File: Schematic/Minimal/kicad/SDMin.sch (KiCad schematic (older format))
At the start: 89 parts

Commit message: Update schematic, order capacitors/resistors/headers and list their size in HW
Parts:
- removed C?: 4.7uF, symbol C_Small
- removed C?: 0.22uF, symbol C_Small
- removed C?: 10uF, symbol C_Small
- removed C?: 100nF, symbol C_Small
- removed SW? (x7): SW_PUSH, symbol SW_PUSH
- removed U?: LSM303DTR, symbol LSM303DTR
- added SW2, SW3, SW4, SW6, SW7, SW8, SW9: SW_PUSH, Buttons_Switches_ThroughHole:SW_PUSH_SMALL, symbol SW_PUSH
- C1, C2: renamed from C?; footprint (none) -> Capacitors_ThroughHole:C_Radial_D5_L11_P2.5
- C11, C13, C15, C4, C7: renamed from C?; value 100nF -> 0.1uF
- C27: renamed from C?; value 4700pF -> 4.7nF
- SW1: renamed from SW?; footprint (none) -> Buttons_Switches_ThroughHole:SW_PUSH_SMALL
- U12: renamed from U?; footprint (none) -> Housings_SOIC:SOIC-28_7.5x17.9mm_Pitch1.27mm
- U8: renamed from U?; footprint (none) -> Housings_DFN_QFN:QFN-16-1EP_3x3mm_Pitch0.5mm
- gave numbers to parts that had none: 66
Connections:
- net labels removed: PB12_MAG-INT1, PB13_MAG-INT2, PB15_MAG-SDI, PB3_dbg, PC2_MAG-SDO
- wire segments 294 -> 262
- no-connect marks 0 -> 39

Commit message: Finish schematic, finish drawing footprints, associate all parts to footprints, get a reading from the GPS.
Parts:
- added C30: 0.1uF, Capacitors_SMD:C_0805_HandSoldering, symbol C_Small
- BT1: footprint (none) -> con-trougnouf:18650BatteryHolder
- C10, C12, C14, C16, C17, C3, C5, C6, C8, C9: footprint (none) -> Capacitors_ThroughHole:C_Radial_D5_L11_P2.5
- C11, C13, C15, C19, C20, C21, C22, C23, C24, C25, C26, C27, C28, C29, C4, C7: footprint (none) -> Capacitors_SMD:C_0805_HandSoldering
- C18: value 100nF -> 0.1uF; footprint (none) -> Capacitors_SMD:C_0805_HandSoldering
- CON1: value SD_Card -> uSD_Card; footprint 10067847-001 -> con-trougnouf:MicroSD; symbol SD_Card -> uSD_Card
- D1, D2, D3: footprint (none) -> LEDs:LED_0603
- L1: value 4.7uF -> 4.7uH; footprint (none) -> Inductors_NEOSID:Neosid_Inductor_SM-NE29_SMD1008
- L2: footprint (none) -> Inductors_NEOSID:Neosid_Inductor_SM-NE29_SMD1008
- P2, P3, P4: footprint (none) -> Pin_Headers:Pin_Header_Straight_1x04
- R1, R10, R11, R12, R13, R14, R15, R16, R17, R18, R19, R2, R20, R21, R22, R3, R4, R5, R6, R7, R8, R9: footprint (none) -> Resistors_SMD:R_0805_HandSoldering
- U10: footprint (none) -> Pin_Headers:Pin_Header_Straight_1x03
- U11: footprint (none) -> BT:RN-52
- U7: footprint Pin_Headers:Pin_Header_Straight_1x05 -> Pin_Headers:Pin_Header_Straight_1x04
- U9: footprint (none) -> Pin_Headers:Pin_Header_Straight_1x05
- X1: footprint (none) -> Crystals:Crystal_HC49-SD_SMD
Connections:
- wire segments 262 -> 263
- no-connect marks 39 -> 38

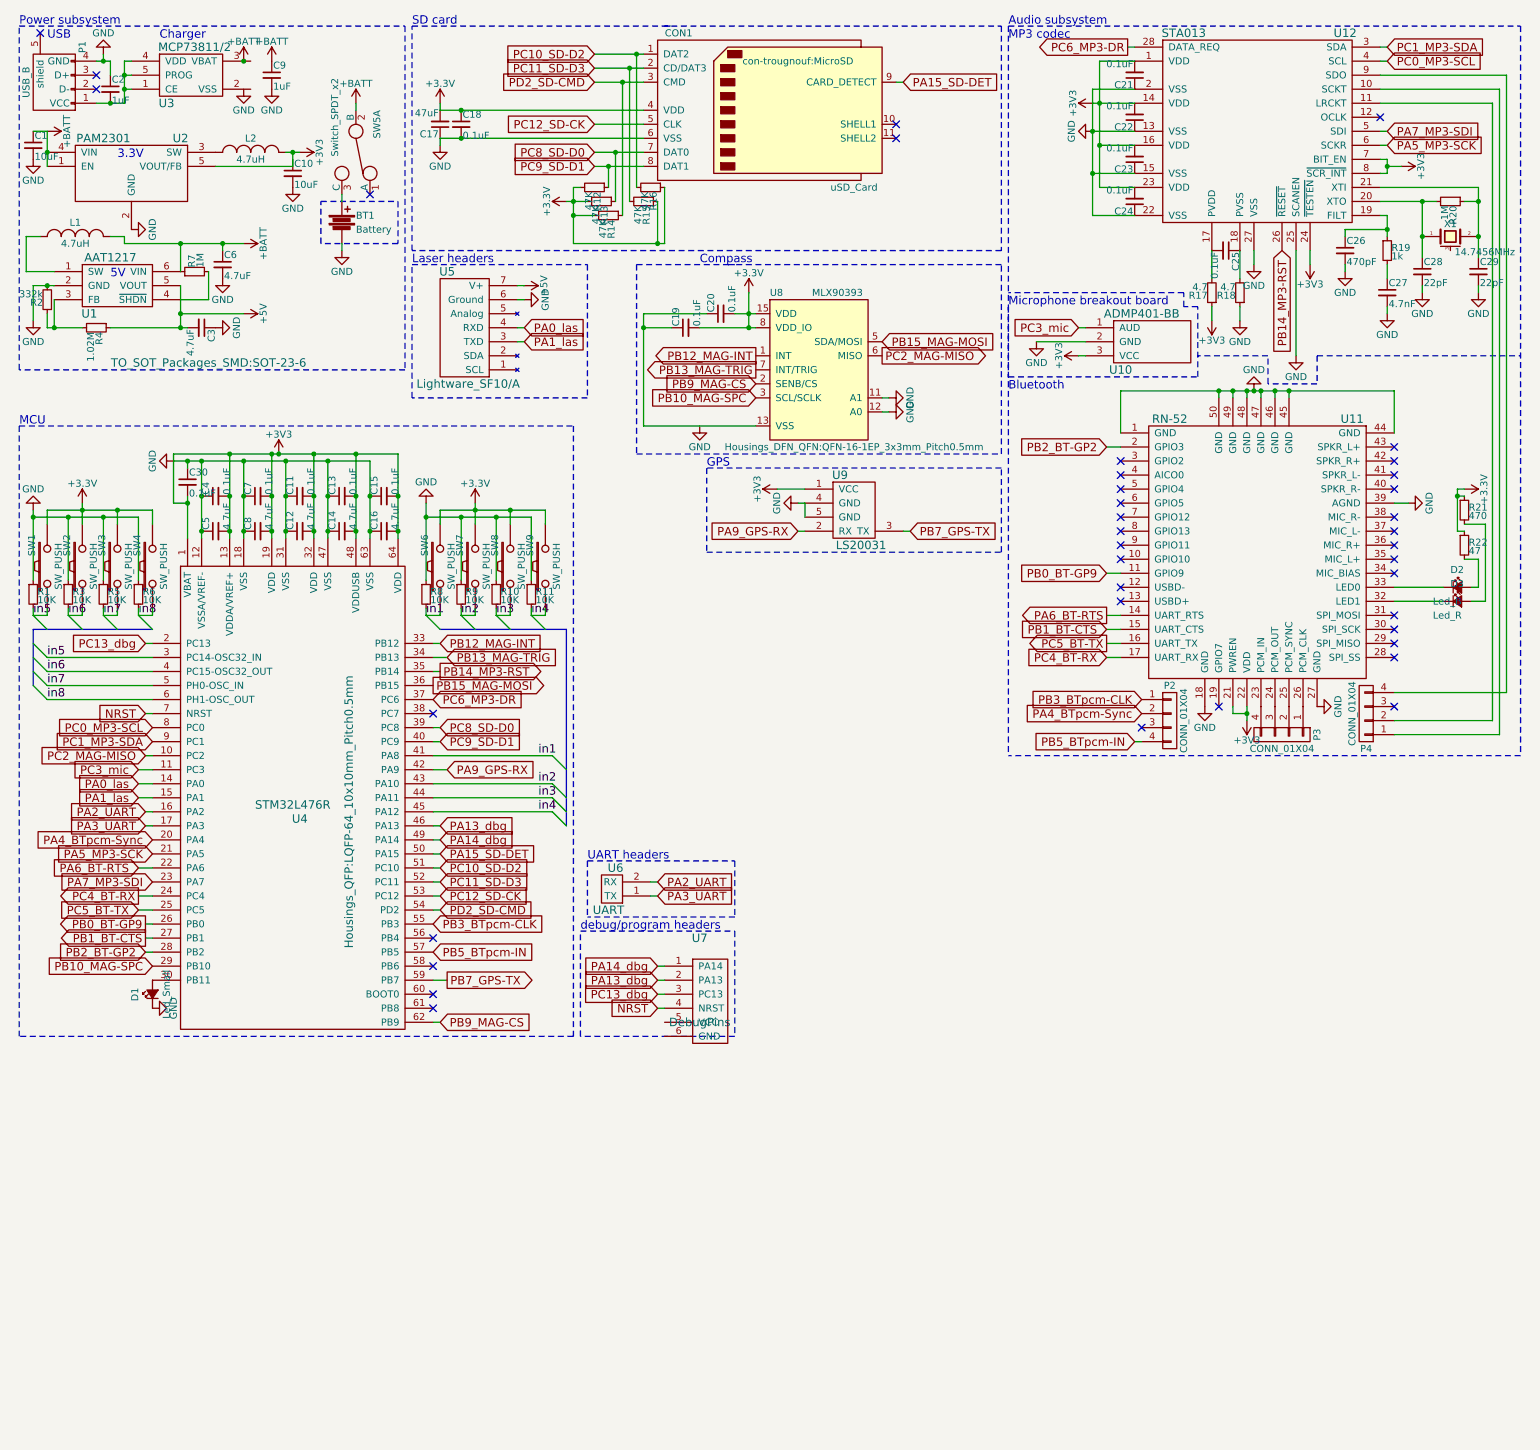
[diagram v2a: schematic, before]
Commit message: Working on the PCB (third attempt). Misc schematic fixes (charger always on)
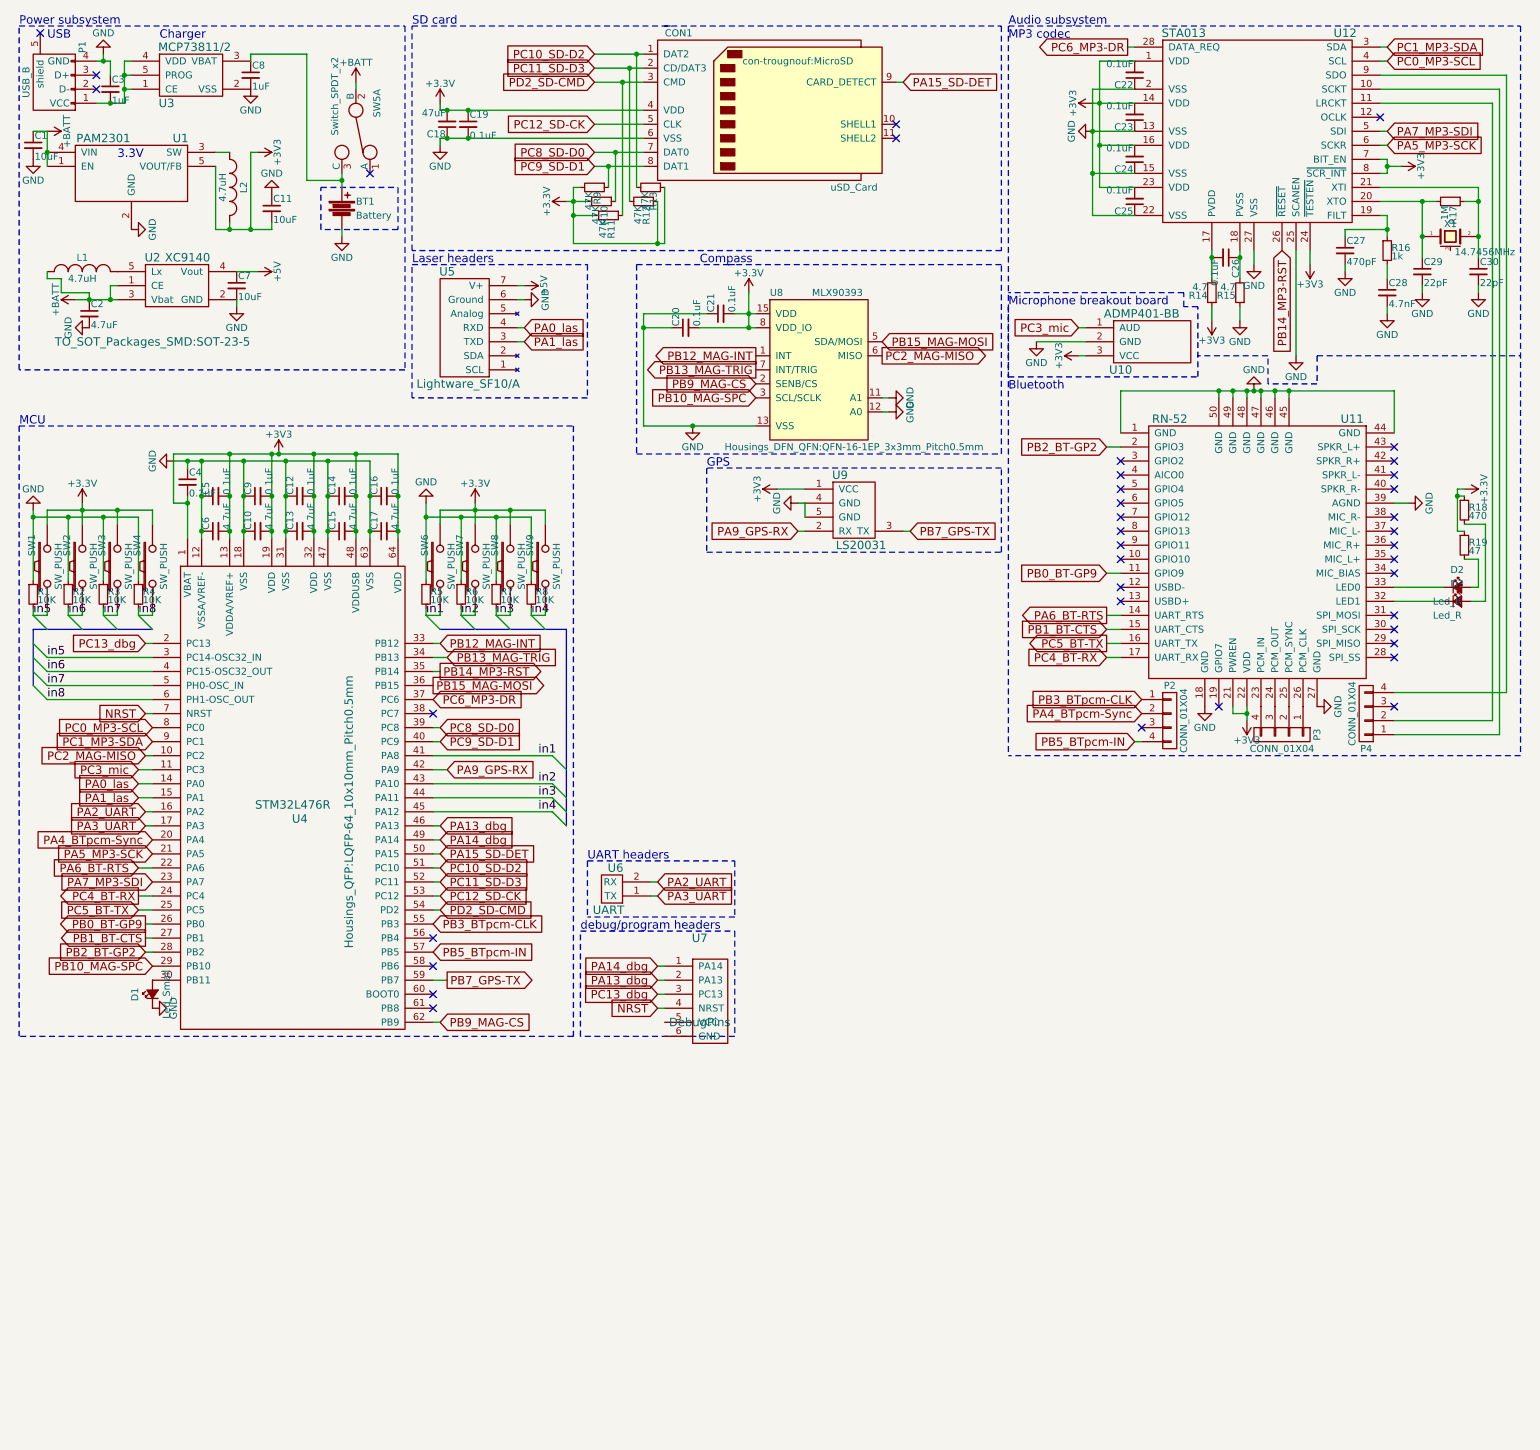
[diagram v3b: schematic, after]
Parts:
- removed C3, C6: 4.7uF, Capacitors_ThroughHole:C_Radial_D5_L11_P2.5, symbol C_Small
- removed R2: 332k, Resistors_SMD:R_0805_HandSoldering, symbol R_Small
- removed R4: 1.02M, Resistors_SMD:R_0805_HandSoldering, symbol R_Small
- removed R7: 1M, Resistors_SMD:R_0805_HandSoldering, symbol R_Small
- removed U1: AAT1217, TO_SOT_Packages_SMD:SOT-23-6, symbol AAT1217
- added C2: 4.7uF, Capacitors_SMD:C_0805_HandSoldering, symbol C_Small
- added C7: 10uF, Capacitors_SMD:C_0805_HandSoldering, symbol C_Small
- added U2: XC9140, TO_SOT_Packages_SMD:SOT-23-5, symbol XC9140
- U10: footprint Pin_Headers:Pin_Header_Straight_1x03 -> con-trougnouf:INMP401-bb
- U9: footprint Pin_Headers:Pin_Header_Straight_1x05 -> con-trougnouf:LS20031+H
- renumbered C8 to C10, C10 to C11, C11 to C12, C12 to C13, C13 to C14, C14 to C15, C15 to C16, C16 to C17, C17 to C18, C18 to C19, C19 to C20, C20 to C21, C21 to C22, C22 to C23, C23 to C24, C24 to C25, C25 to C26, C26 to C27, C27 to C28, C28 to C29, C2 to C3, C29 to C30, C30 to C4, C4 to C5, C5 to C6, C9 to C8, C7 to C9, R13 to R10, R14 to R11, R15 to R12, R16 to R13, R17 to R14, R18 to R15, R19 to R16, R20 to R17, R21 to R18, R22 to R19, R3 to R2, R5 to R3, R6 to R4, R8 to R5, R9 to R6, R10 to R7, R11 to R8, R12 to R9, U2 to U1
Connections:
- net +3V3: now also C11.2
- net +5V: now also C7.1, U2.4 (Vout)
- net +BATT: now also L1.1, C2.1, U2.1 (CE), U2.3 (Vbat); no longer C8.1, L1.2
- net GND: now also C11.1, C20.1, C21.1, U3.2 (VSS), U8.13 (VSS), C2.2, C7.2, U2.2 (GND); no longer C11.2
- net at BT1.1, SW5.3 (C): now also C8.1, U3.3 (VBAT)
- new net: L1.2, U2.5 (Lx)
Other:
- note removed: "5V"
- moved on the sheet: BT1, C11, C18, C19, C26, C8, L1, L2, SW5A

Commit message: Lots of progress on the mPCB
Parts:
- removed SW5: Switch_SPDT_x2, Buttons_Switches_ThroughHole:SW_Micro_SPST, symbol Switch_SPDT_x2
- added C31: 0.1uF, Capacitors_SMD:C_0805_HandSoldering, symbol C_Small
- added P5: CONN_01X03, Pin_Headers:Pin_Header_Straight_1x03, symbol CONN_01X03
- added P6: CONN_01X02, Socket_Strips:Socket_Strip_Straight_1x02, symbol CONN_01X02
- added R20: 10K, Resistors_SMD:R_0805_HandSoldering, symbol R_Small
- added SW5: SW_PUSH, Buttons_Switches_ThroughHole:SW_PUSH_SMALL, symbol SW_PUSH
- U6: footprint Pin_Headers:Pin_Header_Straight_1x02 -> Socket_Strips:Socket_Strip_Straight_1x02
- U7: footprint Pin_Headers:Pin_Header_Straight_1x04 -> Socket_Strips:Socket_Strip_Straight_1x06
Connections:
- net +3V3: now also U7.5 (VCC), C31.2, R20.1
- net +BATT: now also BT1.1, C8.1, U3.3 (VBAT), P5.2 (P2); no longer C1.1, U1.1 (EN), U1.4 (VIN), U2.1 (CE)
- net GND: now also U7.6 (GND), C31.1, SW5.2
- net NRST: now also R20.2, SW5.1
- net at D1.2 (A): now also U4.61 (PB8); no longer U4.30 (PB11)
- net 5VEN: now reaches U4.38 (PC7)
- net 5VEN: now also U2.1 (CE)
- net x-in-1: now reaches U4.56 (PB4)
- net x-in-1: now also P6.2 (P2)
- net x-in-2: now reaches U4.58 (PB6)
- net x-in-2: now also P6.1 (P1)
- net PB0_BT-GP9 renamed PB0_mic
- net PB0_mic: now also U10.1 (AUD); no longer U11.11 (GPIO9)
- net PC3_mic: no longer names the net of U4.11 (PC3)
- net PC3_mic: no longer U10.1 (AUD)
- new net 3VEN: C1.1, P5.1 (P1), U1.1 (EN), U1.4 (VIN)
- new net PB11_BT-GP9: U11.11 (GPIO9), U4.30 (PB11)
- no-connect marks 38 -> 33
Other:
- moved on the sheet: BT1, C8, D1, U7

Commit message: PCB4-23
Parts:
- added C32, C33, C34: 0.1uF, Capacitors_SMD:C_0805_HandSoldering, symbol C_Small
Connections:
- net +3V3: now also C32.1, C33.1, C34.1
- net GND: now also C32.2, C33.2, C34.2
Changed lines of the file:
@@
 Wire Wire Line
 	1200 2400 1050 2400
-Text Label 4350 5450 2    60   ~ 0
+Text Label 3700 5450 2    60   ~ 0
 5VEN
-Wire Wire Line
-	3450 5450 4350 5450
 $Comp
 L R_Small R20
@@
 Connection ~ 5500 5350
 $Comp
-L +BATT #PWR?
+L +BATT #PWR055
 U 1 1 56D36626
 P 800 2450
-F 0 "#PWR?" H 800 2300 50  0001 C CNN
+F 0 "#PWR055" H 800 2300 50  0001 C CNN
 F 1 "+BATT" H 800 2590 50  0000 C CNN
 F 2 "" H 800 2450 50  0000 C CNN
@@
 	0    -1   -1   0
 $EndComp
+$Comp
+L C_Small C32
+U 1 1 56D39376
+P 5050 4550
+F 0 "C32" H 5060 4620 50  0000 L CNN
+F 1 "0.1uF" H 5060 4470 50  0000 L CNN
+F 2 "Capacitors_SMD:C_0805_HandSoldering" H 5050 4550 50  0001 C CNN
+F 3 "" H 5050 4550 50  0000 C CNN
+	1    5050 4550
+	0    -1   -1   0
+$EndComp
+$Comp
+L C_Small C33
+U 1 1 56D39874
+P 5050 4700
+F 0 "C33" H 5060 4770 50  0000 L CNN
+F 1 "0.1uF" H 5060 4620 50  0000 L CNN
+F 2 "Capacitors_SMD:C_0805_HandSoldering" H 5050 4700 50  0001 C CNN
+F 3 "" H 5050 4700 50  0000 C CNN
+	1    5050 4700
+	0    -1   -1   0
+$EndComp
+$Comp
+L +3.3V #PWR056
+U 1 1 56D39A98
+P 4900 4550
+F 0 "#PWR056" H 4900 4400 50  0001 C CNN
+F 1 "+3.3V" H 4900 4690 50  0000 C CNN
+F 2 "" H 4900 4550 50  0000 C CNN
+F 3 "" H 4900 4550 50  0000 C CNN
+	1    4900 4550
+	0    -1   -1   0
+$EndComp
+$Comp
+L +3.3V #PWR057
+U 1 1 56D39BB4
+P 4900 4700
+F 0 "#PWR057" H 4900 4550 50  0001 C CNN
+F 1 "+3.3V" H 4900 4840 50  0000 C CNN
+F 2 "" H 4900 4700 50  0000 C CNN
+F 3 "" H 4900 4700 50  0000 C CNN
+	1    4900 4700
+	0    -1   -1   0
+$EndComp
+$Comp
+L GND #PWR058
+U 1 1 56D39CD0
+P 5200 4550
+F 0 "#PWR058" H 5200 4300 50  0001 C CNN
+F 1 "GND" H 5200 4400 50  0000 C CNN
+F 2 "" H 5200 4550 50  0000 C CNN
+F 3 "" H 5200 4550 50  0000 C CNN
+	1    5200 4550
+	0    -1   -1   0
+$EndComp
+$Comp
+L GND #PWR059
+U 1 1 56D39DEC
+P 5200 4700
+F 0 "#PWR059" H 5200 4450 50  0001 C CNN
+F 1 "GND" H 5200 4550 50  0000 C CNN
+F 2 "" H 5200 4700 50  0000 C CNN
+F 3 "" H 5200 4700 50  0000 C CNN
+	1    5200 4700
+	0    -1   -1   0
+$EndComp
+$Comp
+L C_Small C34
+U 1 1 56D3A0EC
+P 5050 4850
+F 0 "C34" H 5060 4920 50  0000 L CNN
+F 1 "0.1uF" H 5060 4770 50  0000 L CNN
+F 2 "Capacitors_SMD:C_0805_HandSoldering" H 5050 4850 50  0001 C CNN
+F 3 "" H 5050 4850 50  0000 C CNN
+	1    5050 4850
+	0    -1   -1   0
+$EndComp
+$Comp
+L +3.3V #PWR060
+U 1 1 56D3A0F2
+P 4900 4850
+F 0 "#PWR060" H 4900 4700 50  0001 C CNN
+F 1 "+3.3V" H 4900 4990 50  0000 C CNN
+F 2 "" H 4900 4850 50  0000 C CNN
+F 3 "" H 4900 4850 50  0000 C CNN
+	1    4900 4850
+	0    -1   -1   0
+$EndComp
+$Comp
+L GND #PWR061
+U 1 1 56D3A0F8
+P 5200 4850
+F 0 "#PWR061" H 5200 4600 50  0001 C CNN
+F 1 "GND" H 5200 4700 50  0000 C CNN
+F 2 "" H 5200 4850 50  0000 C CNN
+F 3 "" H 5200 4850 50  0000 C CNN
+	1    5200 4850
+	0    -1   -1   0
+$EndComp
+Wire Wire Line
+	4900 4550 4950 4550
+Wire Wire Line
+	4900 4700 4950 4700
+Wire Wire Line
+	4900 4850 4950 4850
+Wire Wire Line
+	5150 4850 5200 4850
+Wire Wire Line
+	5150 4700 5200 4700
+Wire Wire Line
+	5150 4550 5200 4550
+Wire Wire Line
+	3700 5450 3450 5450
 $EndSCHEMATC

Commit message: Ordered PCB. Making no progress on the compass.
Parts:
- added C35, C36, C37: C_Small, symbol C_Small
- added JP1, JP2: Jumper_NC_Small, Pin_Headers:Pin_Header_Straight_1x02, symbol Jumper_NC_Small
- added M1: LaserBracket, con-trougnouf:LaserHolder, symbol LaserBracket
- P5: value CONN_01X03 -> CONN_01X02; footprint Pin_Headers:Pin_Header_Straight_1x03 -> Pin_Headers:Pin_Header_Straight_1x02; symbol CONN_01X03 -> CONN_01X02
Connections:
- net +3V3: now also JP2.2; no longer C11.2, L2.2, U1.5 (VOUT/FB)
- net +5V: now also JP1.2; no longer C7.1, U2.4 (Vout)
- net +BATT: now also C1.1, U1.4 (VIN)
- net 3VEN: no longer C1.1, U1.4 (VIN)
- net GND: no longer U11.39 (AGND)
- new net: C11.2, JP2.1, L2.2, U1.5 (VOUT/FB)
- new net: C7.1, JP1.1, U2.4 (Vout)
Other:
- note added: "misc"
- moved on the sheet: C31, C32, C33, C34, R20, SW5
